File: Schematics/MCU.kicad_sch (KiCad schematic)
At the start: 19 parts, among them SW1 SW_Push, SW2 SW_Push, U1 STM32F405RGTx

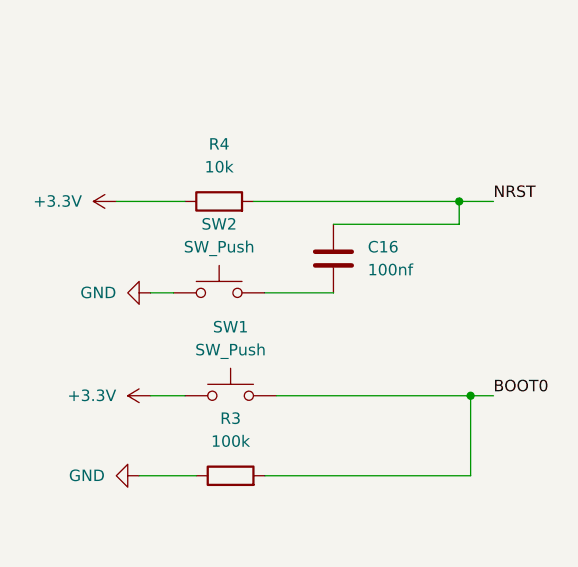
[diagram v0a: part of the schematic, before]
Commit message: fixing duplicate project files and fixing github merge conflict
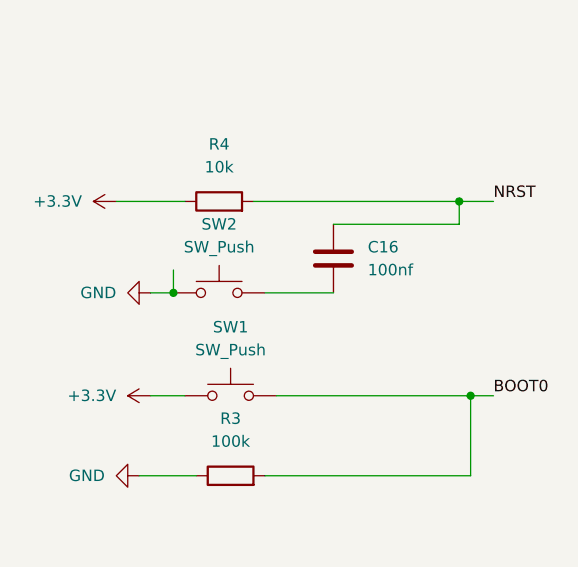
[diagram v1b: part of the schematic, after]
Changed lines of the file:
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@@
+	)
+	(junction
+		(at 33.02 63.5)
+		(diameter 0)
+		(color 0 0 0 0)
 	)
 	(junction
@@
 		)
 		(stroke
+			(width 0)
+			(type default)
+		)
+	)
+	(wire
+		(pts
+			(xy 33.02 63.5) (xy 33.02 60.96)
+		)
+		(stroke

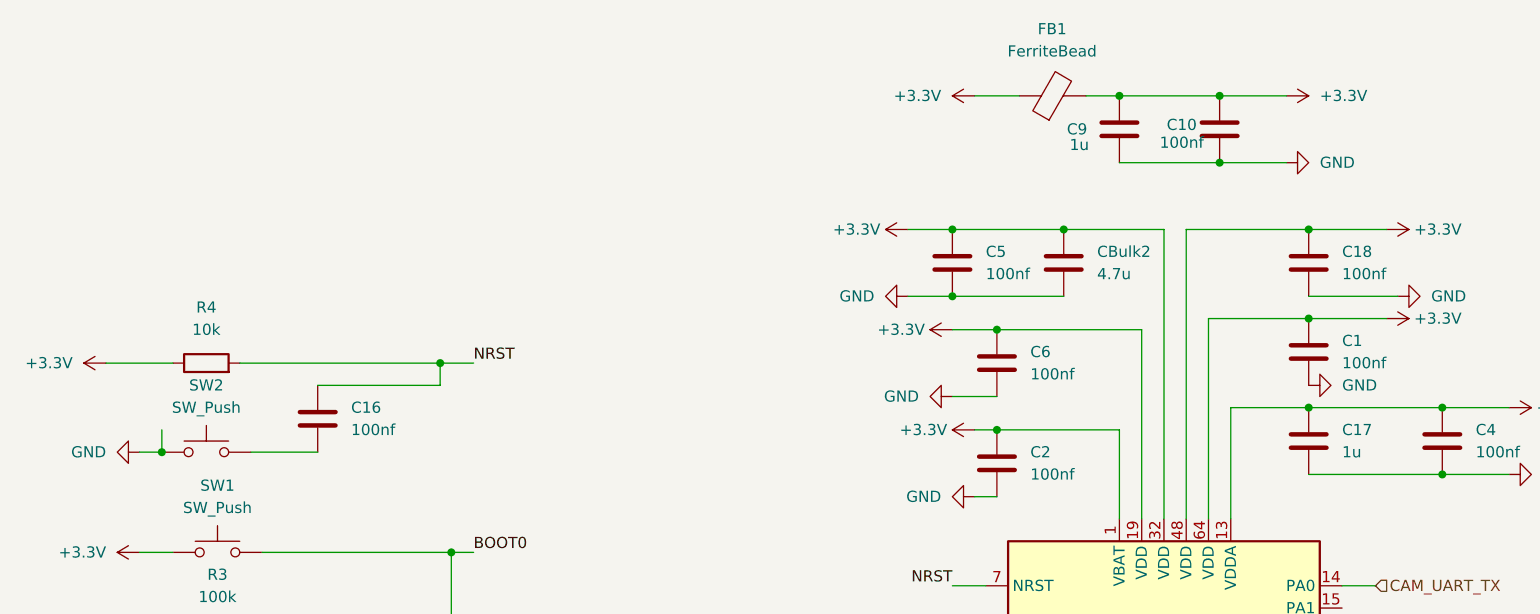
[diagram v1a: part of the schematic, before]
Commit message: fixing routing redefining layout
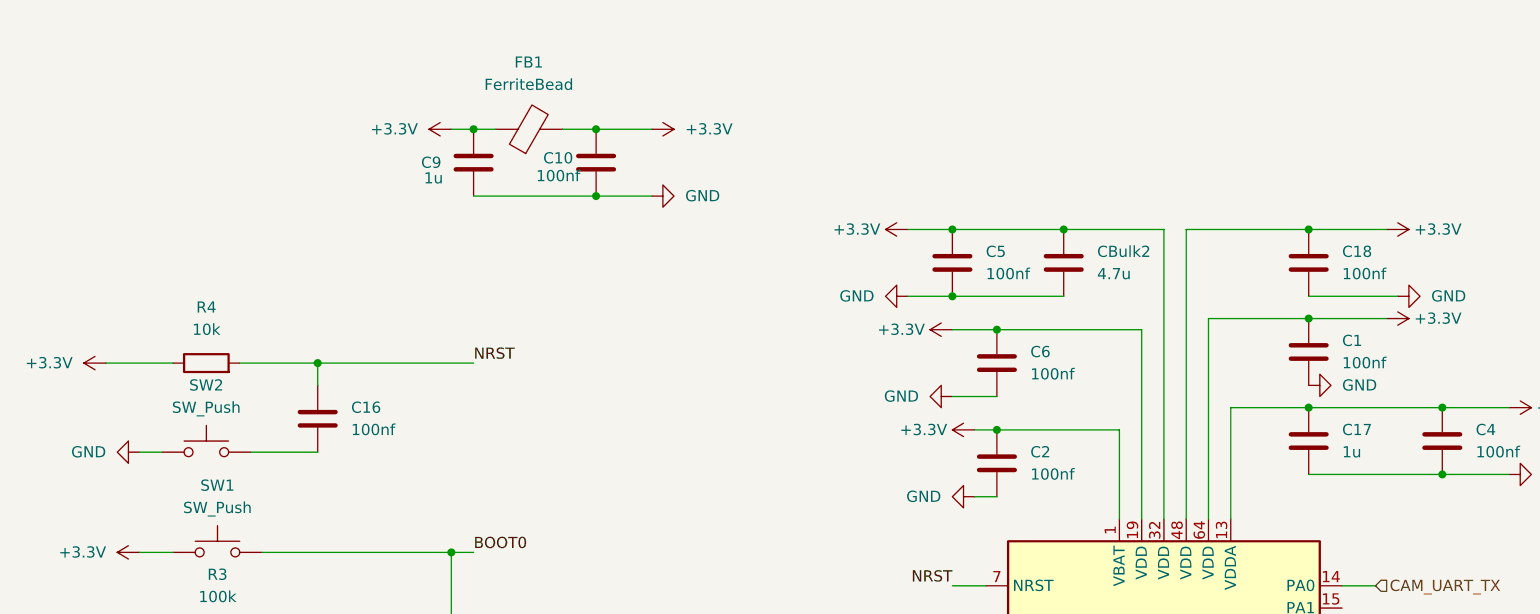
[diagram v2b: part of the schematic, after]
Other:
- moved on the sheet: C10, C9, FB1

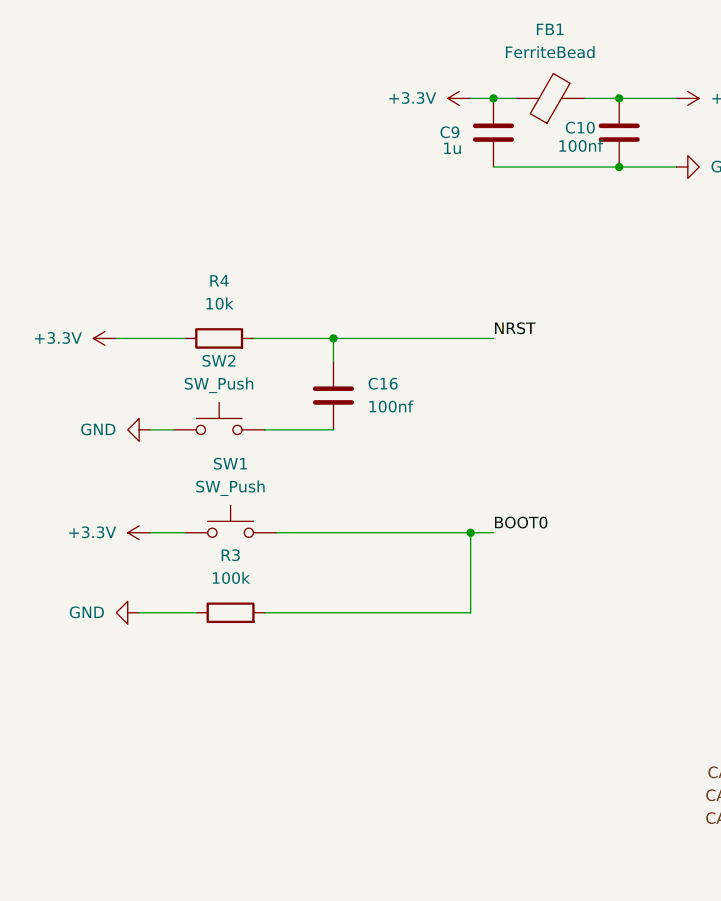
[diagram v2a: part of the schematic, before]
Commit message: Fixed Schematic and PCB refrences everything is connected correctly now
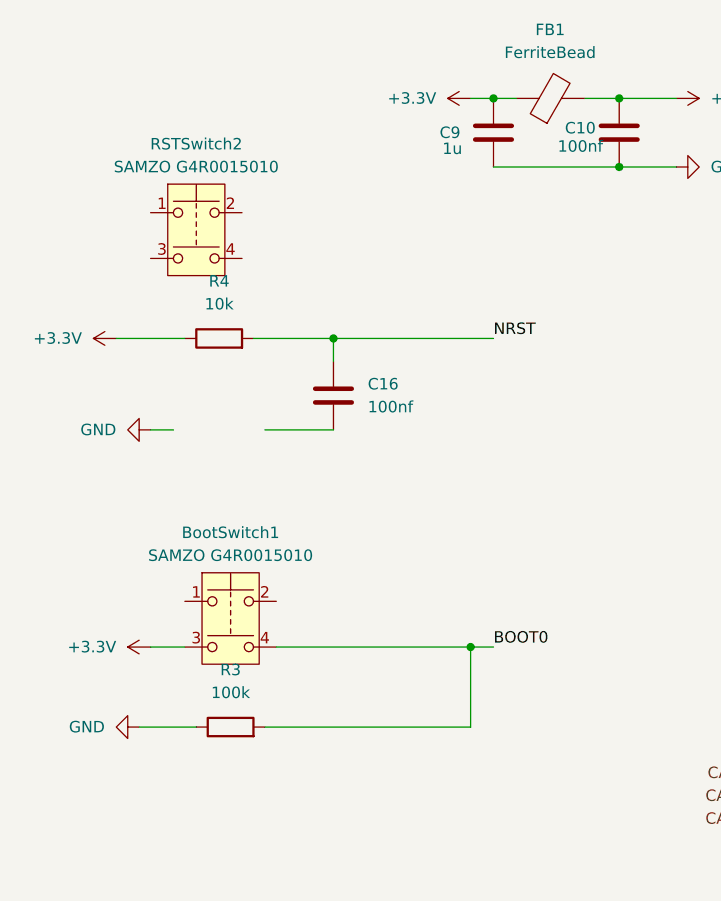
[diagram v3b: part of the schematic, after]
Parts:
- removed SW1, SW2: SW_Push, Button_Switch_THT:SW_PUSH_1P1T_6x3.5mm_H5.0_APEM_MJTP1250, symbol Switch:SW_Push
- added BootSwitch1, RSTSwitch2: SAMZO G4R0015010, myFootprints:SAMZO G4R0015010, symbol Switch:SW_Push_Dual
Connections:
- net +3.3V: now also BootSwitch1.3
- net BOOT0: now also BootSwitch1.4
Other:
- moved on the sheet: R3
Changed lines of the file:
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@@
 	)
 	(junction
-		(at 66.04 74.93)
+		(at 66.04 87.63)
 		(diameter 0)
 		(color 0 0 0 0)
@@
 	(wire
 		(pts
-			(xy 66.04 74.93) (xy 68.58 74.93)
+			(xy 66.04 87.63) (xy 68.58 87.63)
 		)
 		(stroke
@@
 	(wire
 		(pts
-			(xy 44.45 74.93) (xy 66.04 74.93)
+			(xy 44.45 87.63) (xy 66.04 87.63)
 		)
 		(stroke
@@
 	(wire
 		(pts
-			(xy 29.21 83.82) (xy 35.56 83.82)
+			(xy 29.21 96.52) (xy 35.56 96.52)
 		)
 		(stroke
@@
 	(wire
 		(pts
-			(xy 30.48 74.93) (xy 34.29 74.93)
+			(xy 30.48 87.63) (xy 34.29 87.63)
 		)
 		(stroke
@@
 	(wire
 		(pts
-			(xy 66.04 74.93) (xy 66.04 83.82)
+			(xy 66.04 87.63) (xy 66.04 96.52)
 		)
 		(stroke
@@
 	(wire
 		(pts
-			(xy 66.04 83.82) (xy 43.18 83.82)
+			(xy 66.04 96.52) (xy 43.18 96.52)
 		)
 		(stroke
@@
 	)
 	(label "BOOT0"
-		(at 68.58 74.93 0)
+		(at 68.58 87.63 0)
 		(effects
 			(font
@@
 	)
 	(symbol
-		(lib_id "Switch:SW_Push")
-		(at 38.1 63.5 0)
+		(lib_id "Switch:SW_Push_Dual")
+		(at 35.56 41.91 0)
 		(unit 1)
 		(exclude_from_sim no)
@@
 		(dnp no)
 		(fields_autoplaced yes)
-		(property "Reference" "SW2"
-			(at 38.1 55.88 0)
+		(property "Reference" "RSTSwitch2"
+			(at 35.56 31.75 0)
 			(effects
 				(font
@@
 			)
 		)
-		(property "Value" "SW_Push"
-			(at 38.1 58.42 0)
+		(property "Value" "SAMZO G4R0015010"
+			(at 35.56 34.29 0)
 			(effects
 				(font
@@
 			)
 		)
-		(property "Footprint" "Button_Switch_THT:SW_PUSH_1P1T_6x3.5mm_H5.0_APEM_MJTP1250"
-			(at 38.1 58.42 0)
+		(property "Footprint" "myFootprints:SAMZO G4R0015010"
+			(at 35.56 34.29 0)
 			(effects
 				(font
@@
 		)
 		(property "Datasheet" "~"
-			(at 38.1 58.42 0)
+			(at 35.56 41.91 0)
 			(effects
 				(font
@@
 			)
 		)
-		(property "Description" "Push button switch, generic, two pins"
-			(at 38.1 63.5 0)
+		(property "Description" "Push button switch, generic, symbol, four pins"
+			(at 35.56 41.91 0)
 			(effects
 				(font
@@
 		(pin "1"
 		)
+		(pin "3"
+		)
+		(pin "2"
+		)
+		(pin "4"
+		)
+		(instances
+			(project "CameraBoard"
+				(path "/65068a32-f105-4204-b50e-234054c5a6d0/5e494e8c-589b-4110-874f-f4b8b9240b86"
+					(reference "RSTSwitch2")
+					(unit 1)
+				)
+			)
+		)
+	)
+	(symbol
+		(lib_id "Switch:SW_Push_Dual")
+		(at 39.37 85.09 0)
+		(unit 1)
+		(exclude_from_sim no)
+		(in_bom yes)
+		(on_board yes)
+		(dnp no)
+		(fields_autoplaced yes)
+		(property "Reference" "BootSwitch1"
+			(at 39.37 74.93 0)
+			(effects
+				(font
+					(size 1.27 1.27)
+				)
+			)
+		)
+		(property "Value" "SAMZO G4R0015010"
+			(at 39.37 77.47 0)
+			(effects
+				(font
+					(size 1.27 1.27)
+				)
+			)
+		)
+		(property "Footprint" "myFootprints:SAMZO G4R0015010"
+			(at 39.37 77.47 0)
+			(effects
+				(font
+					(size 1.27 1.27)
+				)
+				(hide yes)
+			)
+		)
+		(property "Datasheet" "~"
+			(at 39.37 85.09 0)
+			(effects
+				(font
+					(size 1.27 1.27)
+				)
+				(hide yes)
+			)
+		)
+		(property "Description" "Push button switch, generic, symbol, four pins"
+			(at 39.37 85.09 0)
+			(effects
+				(font
+					(size 1.27 1.27)
+				)
+				(hide yes)
+			)
+		)
+		(pin "1"
+		)
+		(pin "3"
+		)
 		(pin "2"
 		)
+		(pin "4"
+		)
 		(instances
 			(project ""
 				(path "/65068a32-f105-4204-b50e-234054c5a6d0/5e494e8c-589b-4110-874f-f4b8b9240b86"
-					(reference "SW2")
+					(reference "BootSwitch1")
 					(unit 1)
 				)
@@
 	(symbol
 		(lib_id "power:+3.3V")
-		(at 30.48 74.93 90)
+		(at 30.48 87.63 90)
 		(unit 1)
 		(exclude_from_sim no)
@@
 		(fields_autoplaced yes)
 		(property "Reference" "#PWR017"
-			(at 34.29 74.93 0)
+			(at 34.29 87.63 0)
 			(effects
 				(font
@@
 		)
 		(property "Value" "+3.3V"
-			(at 26.67 74.9299 90)
+			(at 26.67 87.6299 90)
 			(effects
 				(font
@@
 		)
 		(property "Footprint" ""
-			(at 30.48 74.93 0)
+			(at 30.48 87.63 0)
 			(effects
 				(font
@@
 		)
 		(property "Datasheet" ""
-			(at 30.48 74.93 0)
+			(at 30.48 87.63 0)
 			(effects
 				(font
@@
 		)
 		(property "Description" "Power symbol creates a global label with name \"+3.3V\""
-			(at 30.48 74.93 0)
+			(at 30.48 87.63 0)
 			(effects
 				(font
@@
 	(symbol
 		(lib_id "power:GND")
-		(at 29.21 83.82 270)
+		(at 29.21 96.52 270)
 		(unit 1)
 		(exclude_from_sim no)
@@
 		(fields_autoplaced yes)
 		(property "Reference" "#PWR018"
-			(at 22.86 83.82 0)
+			(at 22.86 96.52 0)
 			(effects
 				(font
@@
 		)
 		(property "Value" "GND"
-			(at 25.4 83.8199 90)
+			(at 25.4 96.5199 90)
 			(effects
 				(font
@@
 		)
 		(property "Footprint" ""
-			(at 29.21 83.82 0)
+			(at 29.21 96.52 0)
 			(effects
 				(font
@@
 		)
 		(property "Datasheet" ""
-			(at 29.21 83.82 0)
+			(at 29.21 96.52 0)
 			(effects
 				(font
@@
 		)
 		(property "Description" "Power symbol creates a global label with name \"GND\" , ground"
-			(at 29.21 83.82 0)
+			(at 29.21 96.52 0)
 			(effects
 				(font
@@
 	)
 	(symbol
-		(lib_id "Switch:SW_Push")
-		(at 39.37 74.93 0)
-		(unit 1)
-		(exclude_from_sim no)
-		(in_bom yes)
-		(on_board yes)
-		(dnp no)
-		(fields_autoplaced yes)
-		(property "Reference" "SW1"
-			(at 39.37 67.31 0)
-			(effects
-				(font
-					(size 1.27 1.27)
-				)
-			)
-		)
-		(property "Value" "SW_Push"
-			(at 39.37 69.85 0)
-			(effects
-				(font
-					(size 1.27 1.27)
-				)
-			)
-		)
-		(property "Footprint" "Button_Switch_THT:SW_PUSH_1P1T_6x3.5mm_H5.0_APEM_MJTP1250"
-			(at 39.37 69.85 0)
-			(effects
-				(font
-					(size 1.27 1.27)
-				)
-				(hide yes)
-			)
-		)
-		(property "Datasheet" "~"
-			(at 39.37 69.85 0)
-			(effects
-				(font
-					(size 1.27 1.27)
-				)
-				(hide yes)
-			)
-		)
-		(property "Description" "Push button switch, generic, two pins"
-			(at 39.37 74.93 0)
-			(effects
-				(font
-					(size 1.27 1.27)
-				)
-				(hide yes)
-			)
-		)
-		(pin "1"
-		)
-		(pin "2"
-		)
-		(instances
-			(project ""
-				(path "/65068a32-f105-4204-b50e-234054c5a6d0/5e494e8c-589b-4110-874f-f4b8b9240b86"
-					(reference "SW1")
-					(unit 1)
-				)
-			)
-		)
-	)
-	(symbol
 		(lib_id "Device:R")
-		(at 39.37 83.82 90)
+		(at 39.37 96.52 90)
 		(unit 1)
 		(exclude_from_sim no)
@@
 		(fields_autoplaced yes)
 		(property "Reference" "R3"
-			(at 39.37 77.47 90)
+			(at 39.37 90.17 90)
 			(effects
 				(font
@@
 		)
 		(property "Value" "100k"
-			(at 39.37 80.01 90)
+			(at 39.37 92.71 90)
 			(effects
 				(font
@@
 		)
 		(property "Footprint" "Resistor_SMD:R_0805_2012Metric_Pad1.20x1.40mm_HandSolder"
-			(at 39.37 85.598 90)
+			(at 39.37 98.298 90)
 			(effects
 				(font
@@
 		)
 		(property "Datasheet" "~"
-			(at 39.37 83.82 0)
+			(at 39.37 96.52 0)
 			(effects
 				(font
@@
 		)
 		(property "Description" "Resistor"
-			(at 39.37 83.82 0)
+			(at 39.37 96.52 0)
 			(effects
 				(font

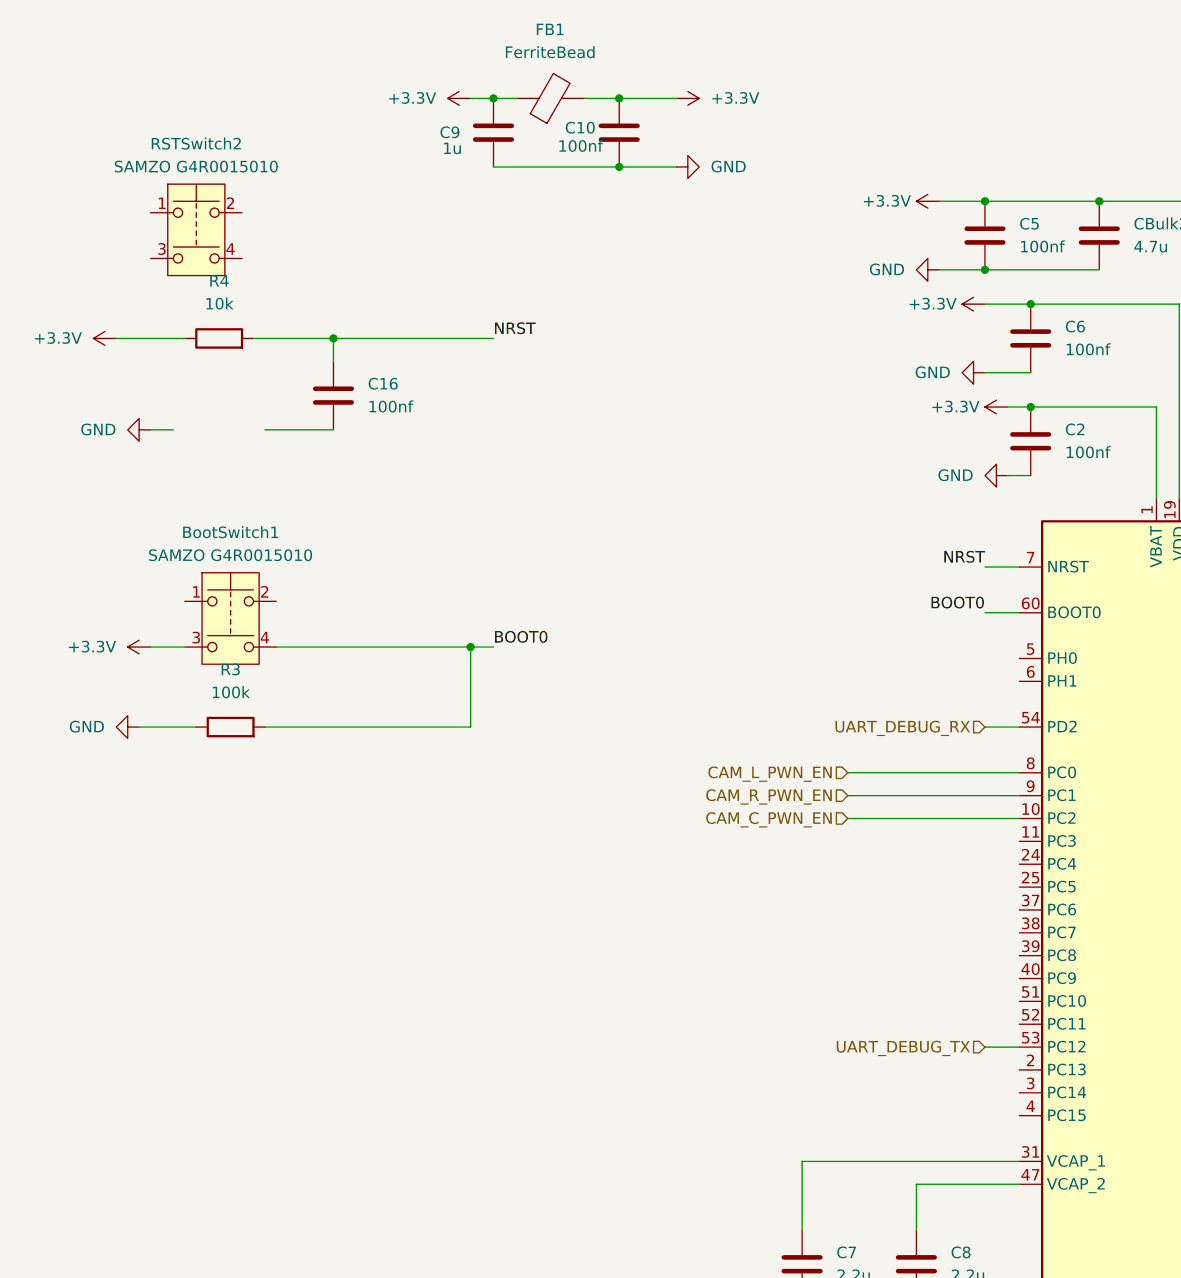
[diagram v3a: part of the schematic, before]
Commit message: fixed all refrences from shematic to pcb and added LED
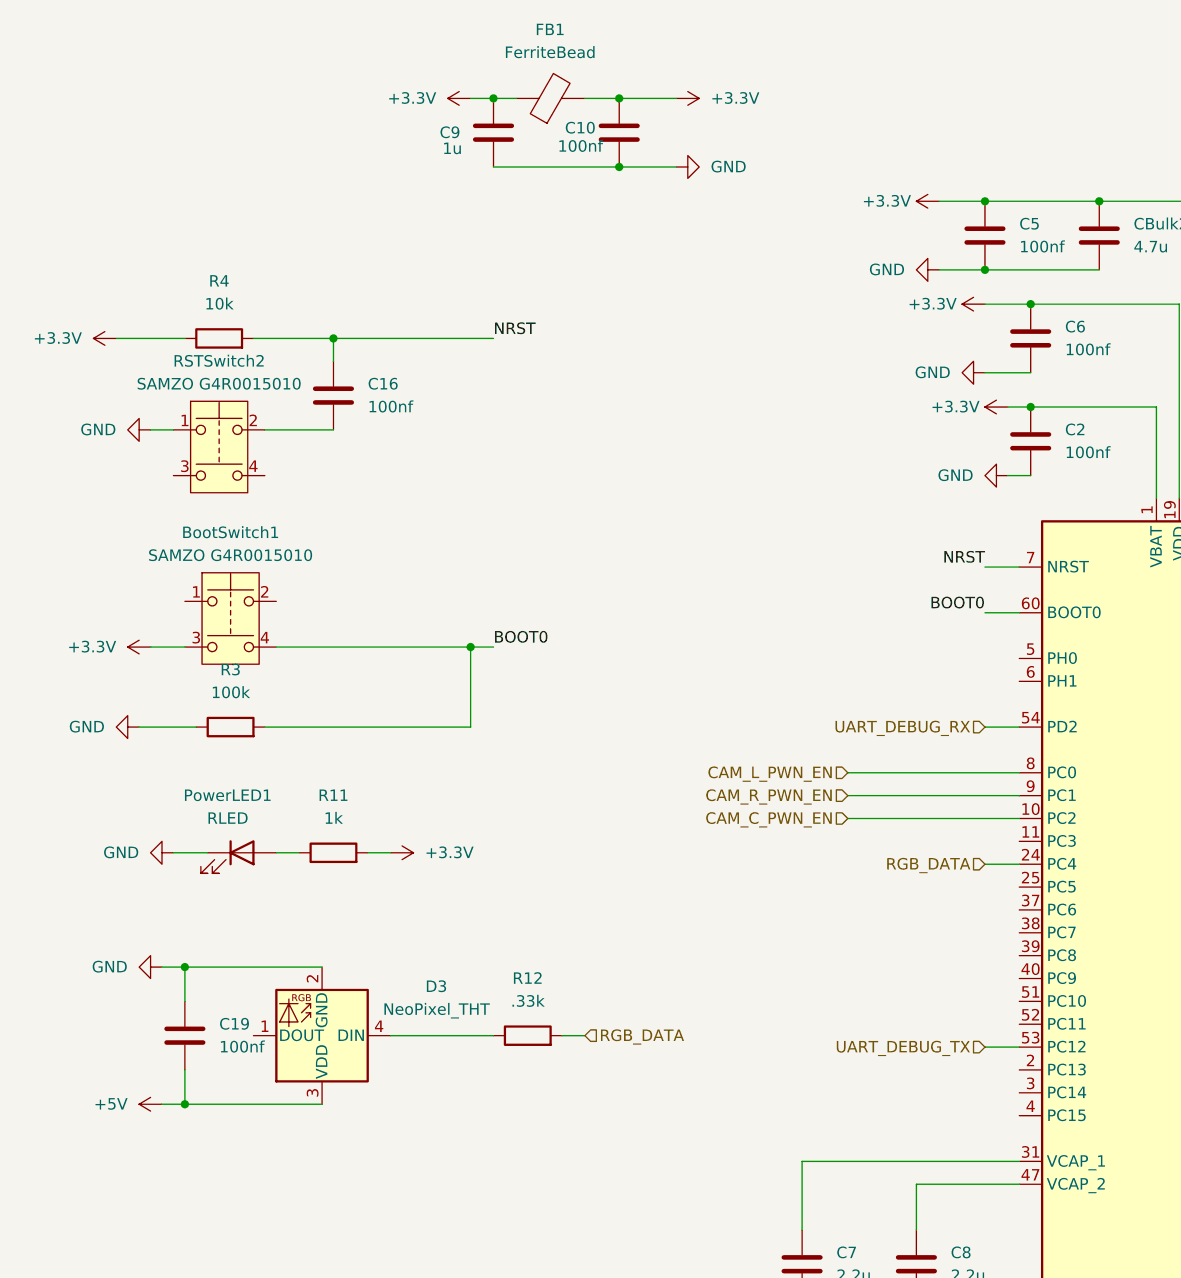
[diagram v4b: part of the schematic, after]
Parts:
- added C19: 100nf, Resistor_SMD:R_0805_2012Metric_Pad1.20x1.40mm_HandSolder, symbol Device:C
- added D3: NeoPixel_THT, LED_SMD:LED_Kingbright_AAA3528ESGCT, symbol LED:NeoPixel_THT
- added PowerLED1: RLED, LED_SMD:LED_0603_1608Metric_Pad1.05x0.95mm_HandSolder, symbol Device:LED
- added R11: 1k, Resistor_SMD:R_0805_2012Metric_Pad1.20x1.40mm_HandSolder, symbol Device:R
- added R12: .33k, Resistor_SMD:R_0805_2012Metric_Pad1.20x1.40mm_HandSolder, symbol Device:R
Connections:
- net +3.3V: now also R11.2
- net GND: now also RSTSwitch2.1, C19.1, D3.2 (GND), PowerLED1.1 (K)
- net at RSTSwitch2.2: now also C16.2
- net RGB_DATA: now reaches U1.24 (PC4)
- net RGB_DATA: now also R12.2
- new net: PowerLED1.2 (A), R11.1
- new net: D3.4 (DIN), R12.1
- new net +5V: C19.2, D3.3 (VDD)
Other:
- moved on the sheet: RSTSwitch2
